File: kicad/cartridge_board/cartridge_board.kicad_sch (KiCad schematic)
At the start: 3 parts, among them J1 Conn_02x04_Odd_Even, U1 ATtiny10

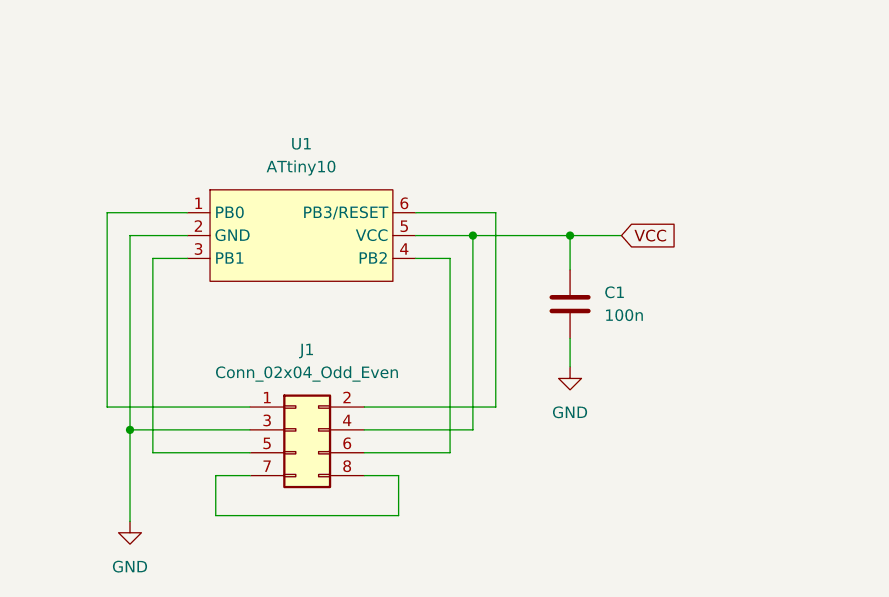
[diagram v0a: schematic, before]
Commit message: flip cartridge pcb
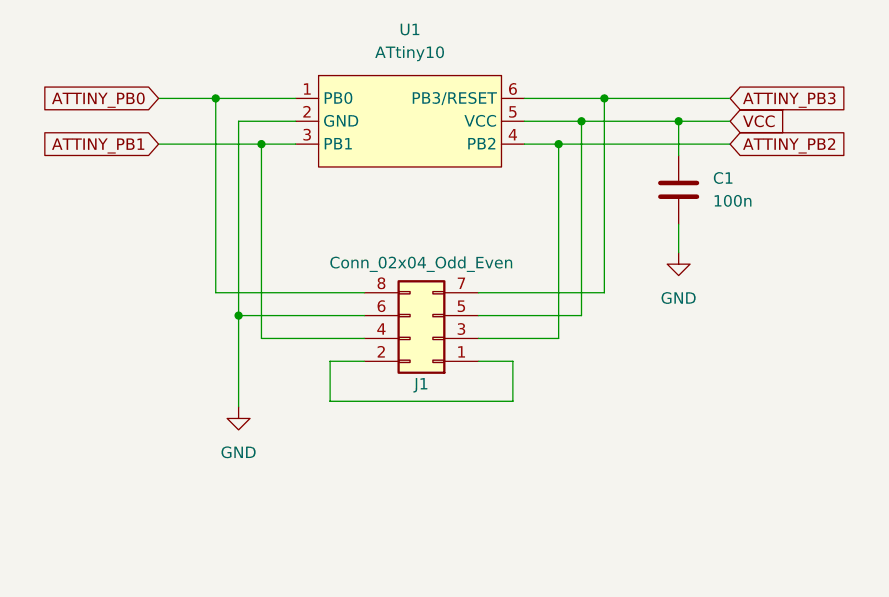
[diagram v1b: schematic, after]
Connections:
- net GND: now also J1.6 (Pin_6); no longer J1.3 (Pin_3)
- net VCC: now also J1.5 (Pin_5); no longer J1.4 (Pin_4)
- net at J1.1 (Pin_1): now also J1.2 (Pin_2); no longer U1.1 (PB0)
- net ATTINY_PB3: now reaches U1.6 (PB3/RESET)
- net ATTINY_PB3: now also J1.7 (Pin_7); no longer J1.2 (Pin_2)
- net ATTINY_PB1: now reaches U1.3 (PB1)
- net ATTINY_PB1: now also J1.4 (Pin_4); no longer J1.5 (Pin_5)
- net ATTINY_PB2: now reaches U1.4 (PB2)
- net ATTINY_PB2: now also J1.3 (Pin_3); no longer J1.6 (Pin_6)
- net ATTINY_PB0: now reaches J1.8 (Pin_8)
- net ATTINY_PB0: now also U1.1 (PB0); no longer J1.7 (Pin_7)
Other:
- moved on the sheet: C1, J1, U1
